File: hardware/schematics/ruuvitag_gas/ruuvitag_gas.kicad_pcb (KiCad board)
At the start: 4 copper layers, 45 x 45 mm, 66 parts, among them P19 TP, P20 TP, P21 TP, P22 TP, P5 RUUVI_BATTERY_CLIP, SW1 SKRKAEE020, U1 nRF52832-QFAA, U2 DPS310XTSA1, U3 SHTC3, U4 LIS2DH12, Y1 FC-135 32.768KHZ ±20PPM,9.0PF, Y2 Q22FA12800025 CRYSTAL 32MHz ±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

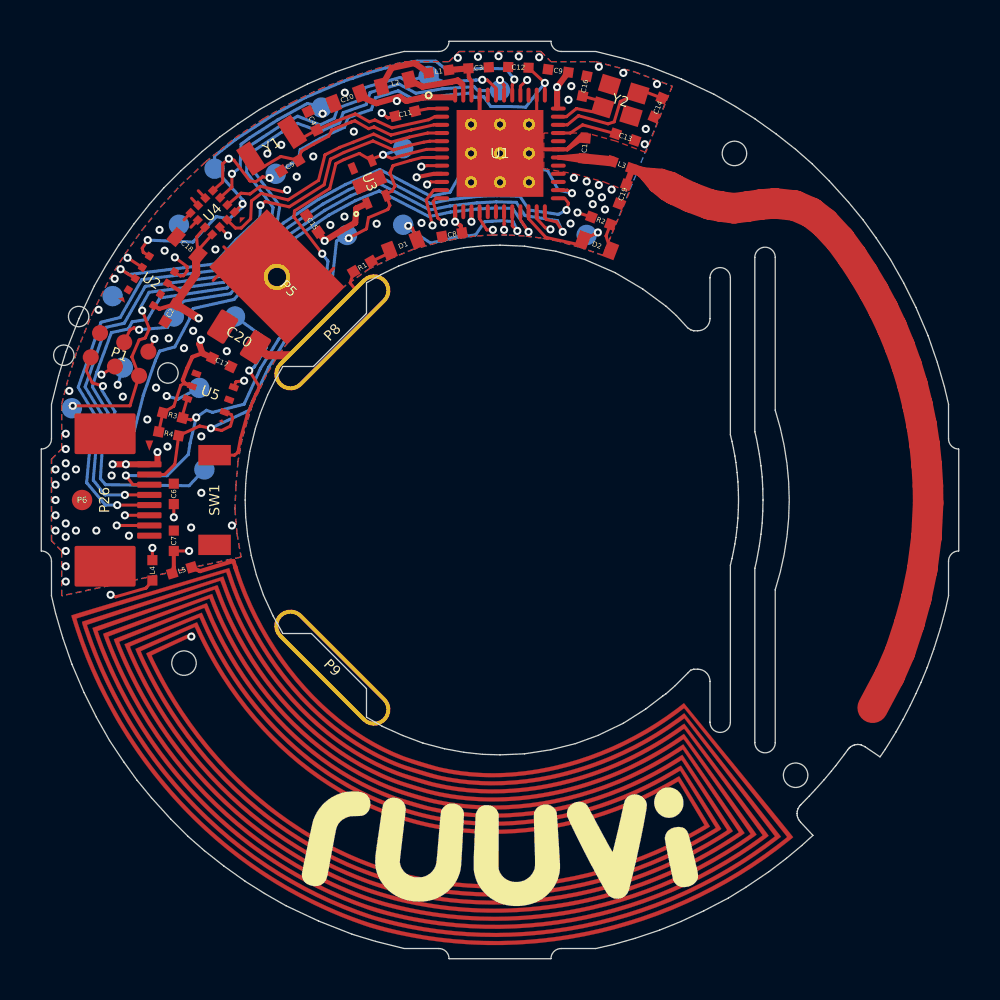
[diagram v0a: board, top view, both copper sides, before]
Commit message: chore(hardware): ruuvitag_gas nach KiCad 9 migriert
GUI-Migration in KiCad 9.0.7 abgeschlossen:
- ruuvitag_gas.sch -> ruuvitag_gas.kicad_sch (Format 20250114), alle Bauteile
  und Netze uebernommen, Symbole aus ruuvitag_gas-cache.lib aufgeloest
- ruuvitag_gas.kicad_pcb ins v9-Format konvertiert (Zonen neu gefuellt)
- .kicad_pro von KiCad aktualisiert, .kicad_prl ergaenzt
- tote Legacy-ruuvitag_gas.sch entfernt

Baseline (unveraendert ggue. Rev.B8):
- ERC: 245 Meldungen (endpoint_off_grid vom 50-mil-Altraster,
  power_pin_not_driven an GPIO-Sensor-Rails, footprint_link_issues RuuviTag-Lib)
- DRC: 245 Meldungen, 0 unverbundene Elemente -> Netzliste intakt

Naechster Schritt: Phase 2 (Sensor-Rueckbau TMP117/DPS310/LIS2DH12 + HX711).

Co-Authored-By: Claude Sonnet 5 <noreply@anthropic.com>
Claude-Session: https://claude.ai/code/session_01TRyZtBjoMYjan8UmtLoPnv
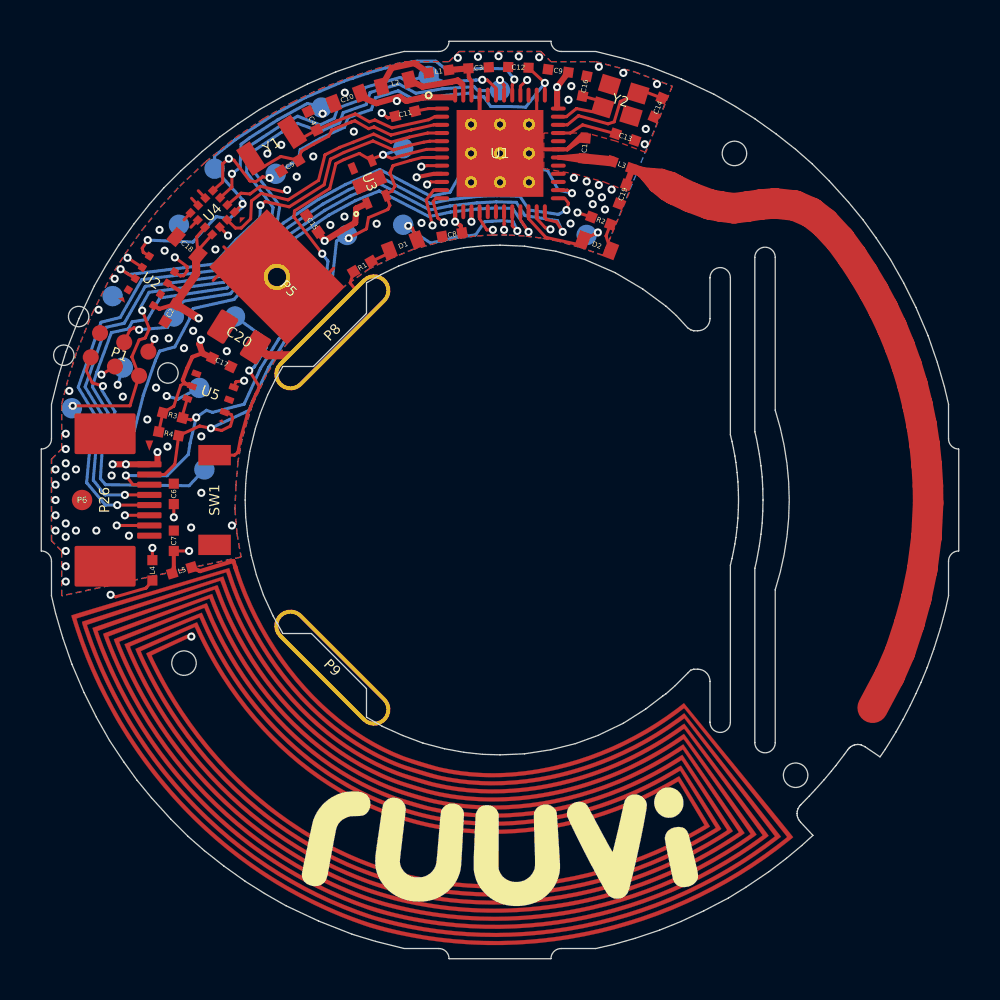
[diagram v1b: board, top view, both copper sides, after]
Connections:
- net /~BUTTON renamed /~{BUTTON}
- net /~LED1 renamed /~{LED1}
- net /~LED2 renamed /~{LED2}
- net /~SPI_ACC_CS renamed /~{SPI_ACC_CS}
- net /~SPI_PRESS_CS renamed /~{SPI_PRESS_CS}
- net /~TMP_ALERT renamed /~{TMP_ALERT}
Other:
- net class Default removed
